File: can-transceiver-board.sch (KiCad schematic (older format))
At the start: 5 parts, among them K1 JMP, P1 CONN_5, U1 MAX3051

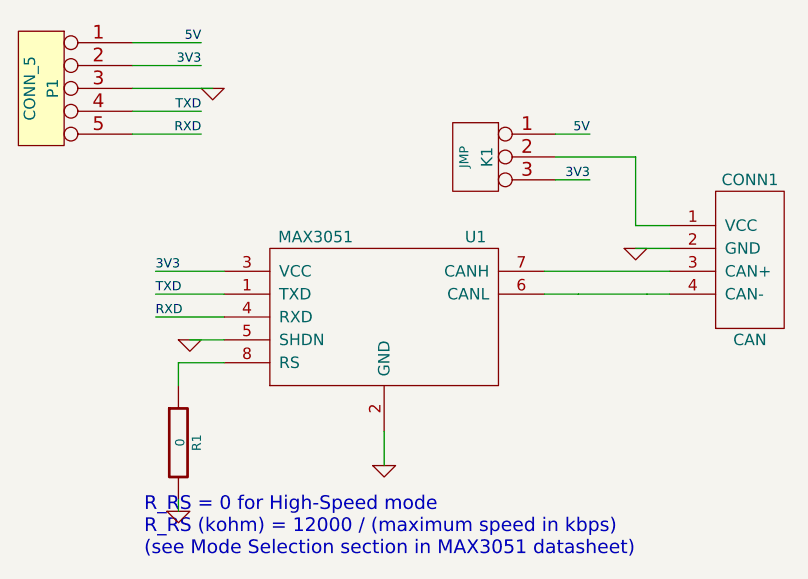
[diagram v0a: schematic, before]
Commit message: Improved GND routing, added CAN terminal resistor pin.
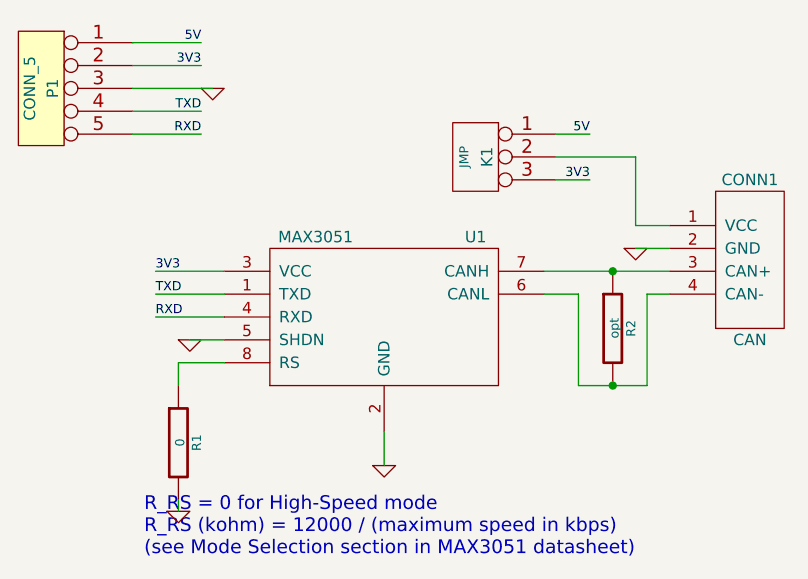
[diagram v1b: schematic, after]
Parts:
- added R2: opt, symbol R
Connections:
- net at CONN1.4 (CAN-), U1.6 (CANL): now also R2.2
- net at CONN1.3 (CAN+), U1.7 (CANH): now also R2.1
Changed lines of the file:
@@
 Text Notes 3600 4500 0    60   ~ 0
 R_RS = 0 for High-Speed mode\nR_RS (kohm) = 12000 / (maximum speed in kbps)\n(see Mode Selection section in MAX3051 datasheet)
-Wire Wire Line
-	3750 3750 3750 3650
-Wire Wire Line
-	3750 3650 3950 3650
-Wire Wire Line
-	3750 4250 3750 4300
-Wire Wire Line
-	4650 4100 4650 3950
-Wire Wire Line
-	5350 3250 5900 3250
-Wire Wire Line
-	5500 3350 5800 3350
-Wire Wire Line
-	5500 3350 5500 3350
-Wire Wire Line
-	5500 3350 5350 3350
-Wire Wire Line
-	3550 2450 3900 2450
-Wire Wire Line
-	3800 3550 3950 3550
-Wire Wire Line
-	3650 3350 3950 3350
-Wire Wire Line
-	3650 3450 3950 3450
-Wire Wire Line
-	3650 3250 3950 3250
-Wire Wire Line
-	5800 3350 5800 3350
-Wire Wire Line
-	5800 3350 5900 3350
-Wire Wire Line
-	5750 3050 5900 3050
 $Comp
 L GND #PWR05
@@
 	1    0    0    -1
 $EndComp
-Wire Wire Line
-	5900 3150 5750 3150
 $Comp
 L CAN CONN1
@@
 	-1   0    0    -1
 $EndComp
-Wire Wire Line
-	3550 2250 3850 2250
-Wire Wire Line
-	3550 2350 3850 2350
 Text Label 3850 2250 2    40   ~ 0
 5V
 Text Label 3850 2350 2    40   ~ 0
 3V3
-Wire Wire Line
-	5750 2750 5750 3050
-Wire Wire Line
-	5400 2750 5750 2750
-Wire Wire Line
-	5550 2850 5400 2850
-Wire Wire Line
-	5400 2650 5550 2650
 $Comp
 L CONN_3 K1
@@
 Text Label 5550 2650 2    40   ~ 0
 5V
-Wire Wire Line
-	3550 2550 3850 2550
-Wire Wire Line
-	3850 2650 3550 2650
 Text Label 3850 2550 2    40   ~ 0
 TXD
@@
 Text Label 3650 3350 0    40   ~ 0
 TXD
+$Comp
+L R R2
+U 1 1 544A0FD2
+P 5650 3500
+F 0 "R2" V 5730 3500 40  0000 C CNN
+F 1 "opt" V 5657 3501 40  0000 C CNN
+F 2 "" V 5580 3500 30  0000 C CNN
+F 3 "" H 5650 3500 30  0000 C CNN
+	1    5650 3500
+	1    0    0    -1
+$EndComp
+Wire Wire Line
+	3750 3750 3750 3650
+Wire Wire Line
+	3750 3650 3950 3650
+Wire Wire Line
+	3750 4250 3750 4300
+Wire Wire Line
+	4650 4100 4650 3950
+Wire Wire Line
+	5350 3250 5900 3250
+Wire Wire Line
+	5350 3350 5500 3350
+Wire Wire Line
+	3550 2450 3900 2450
+Wire Wire Line
+	3800 3550 3950 3550
+Wire Wire Line
+	3650 3350 3950 3350
+Wire Wire Line
+	3650 3450 3950 3450
+Wire Wire Line
+	3650 3250 3950 3250
+Wire Wire Line
+	5800 3350 5900 3350
+Wire Wire Line
+	5750 3050 5900 3050
+Wire Wire Line
+	5900 3150 5750 3150
+Wire Wire Line
+	3550 2250 3850 2250
+Wire Wire Line
+	3550 2350 3850 2350
+Wire Wire Line
+	5750 2750 5750 3050
+Wire Wire Line
+	5400 2750 5750 2750
+Wire Wire Line
+	5550 2850 5400 2850
+Wire Wire Line
+	5400 2650 5550 2650
+Wire Wire Line
+	3550 2550 3850 2550
+Wire Wire Line
+	3850 2650 3550 2650
+Connection ~ 5650 3250
+Wire Wire Line
+	5800 3750 5800 3350
+Wire Wire Line
+	5500 3750 5800 3750
+Wire Wire Line
+	5500 3350 5500 3750
+Connection ~ 5650 3750
 $EndSCHEMATC
